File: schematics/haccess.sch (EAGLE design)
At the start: 41 parts, among them IC1 ATMEGA32U2-TQFP, IC2 REG1117, SW1 SPST_TACT-EVQQ2

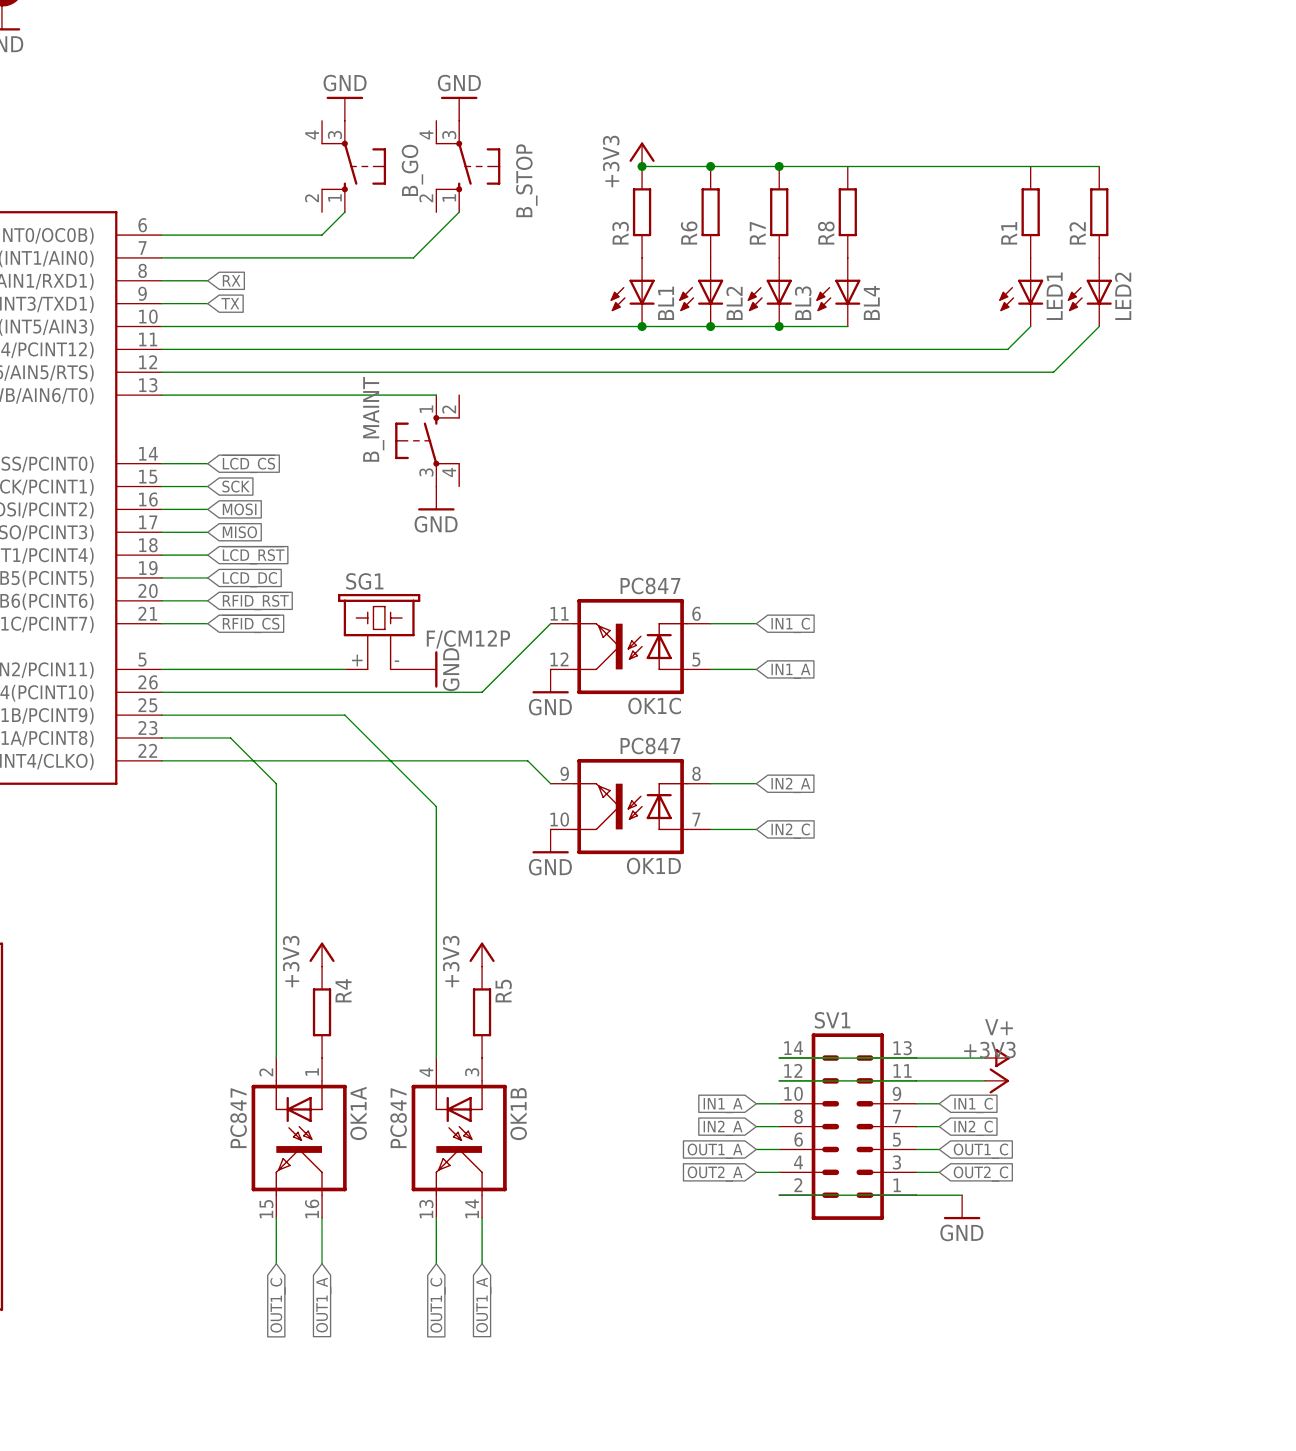
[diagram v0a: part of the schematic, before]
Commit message: First version of haccess PCB
Has components in correct places, some minimal routing.

Modified pattress plate to add correclty spaced holes for bolting haccess to plate.
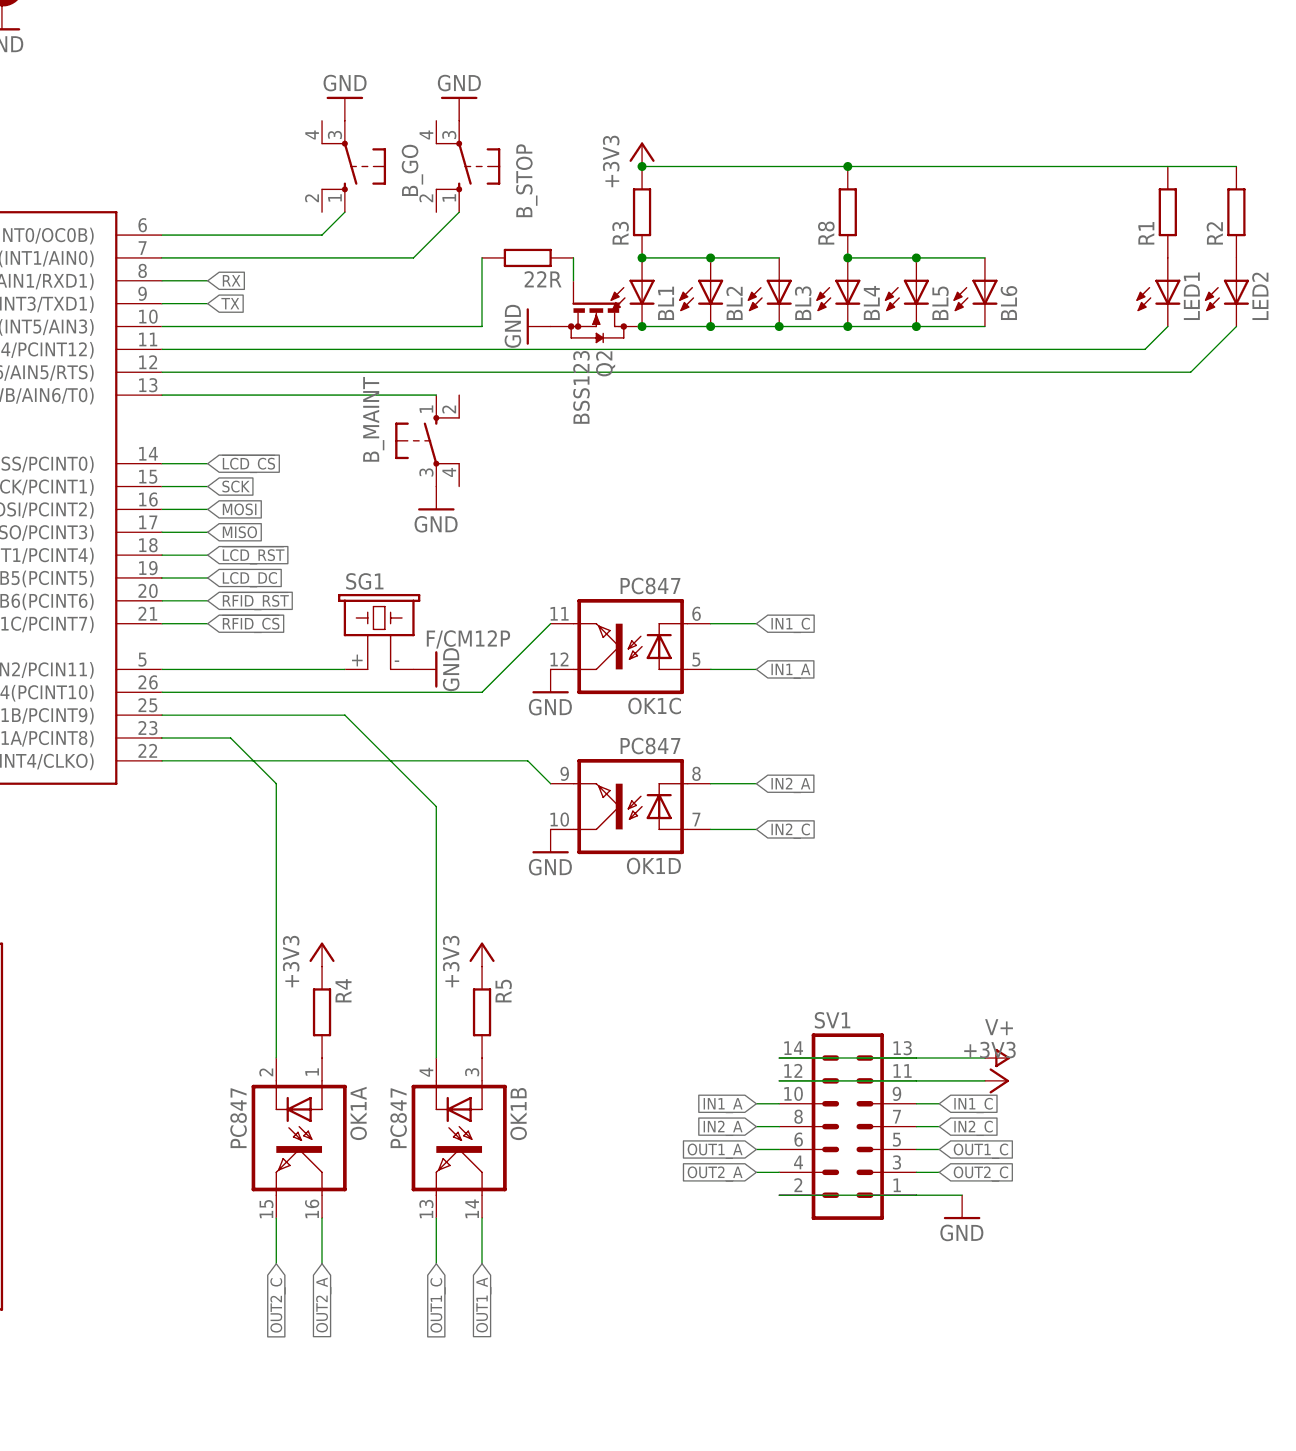
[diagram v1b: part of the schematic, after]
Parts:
- removed R6, R7: (no value), rcl:R-EU_R0805
- added 22R: (no value), rcl:R-EU_R0805
- added BL5, BL6: (no value), led:LEDCHIP-LED0805
- added Q2: BSS123, transistor-small-signal:BSS123
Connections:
- net +3V3: no longer R6.2, R7.2
- net GND: now also Q2.S
- net N$18: now also BL5.C, BL6.C, Q2.D; no longer IC1.PD4(INT5/AIN3)
- net N$19: now also BL2.A, BL3.A
- net N$21: now also 22R.2, IC1.PD4(INT5/AIN3); no longer BL2.A, R6.1
- net N$22: now also 22R.1, Q2.G; no longer BL3.A, R7.1
- net N$23: now also BL5.A, BL6.A
- net OUT1_A: no longer OK1A.COL
- net OUT1_C: no longer OK1A.EMIT
- net OUT2_A: now also OK1A.COL
- net OUT2_C: now also OK1A.EMIT
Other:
- moved on the sheet: LED1, LED2, R1, R2

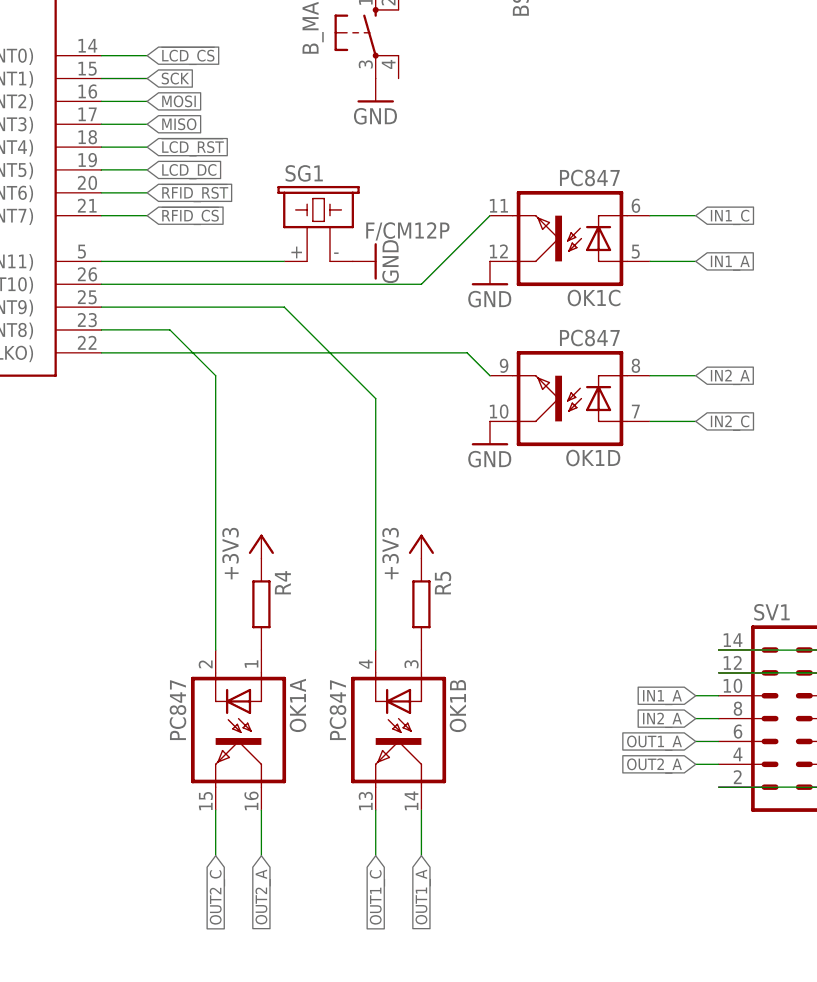
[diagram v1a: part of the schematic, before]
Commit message: Imported DXF of outline, got all important tuff into place, began routing
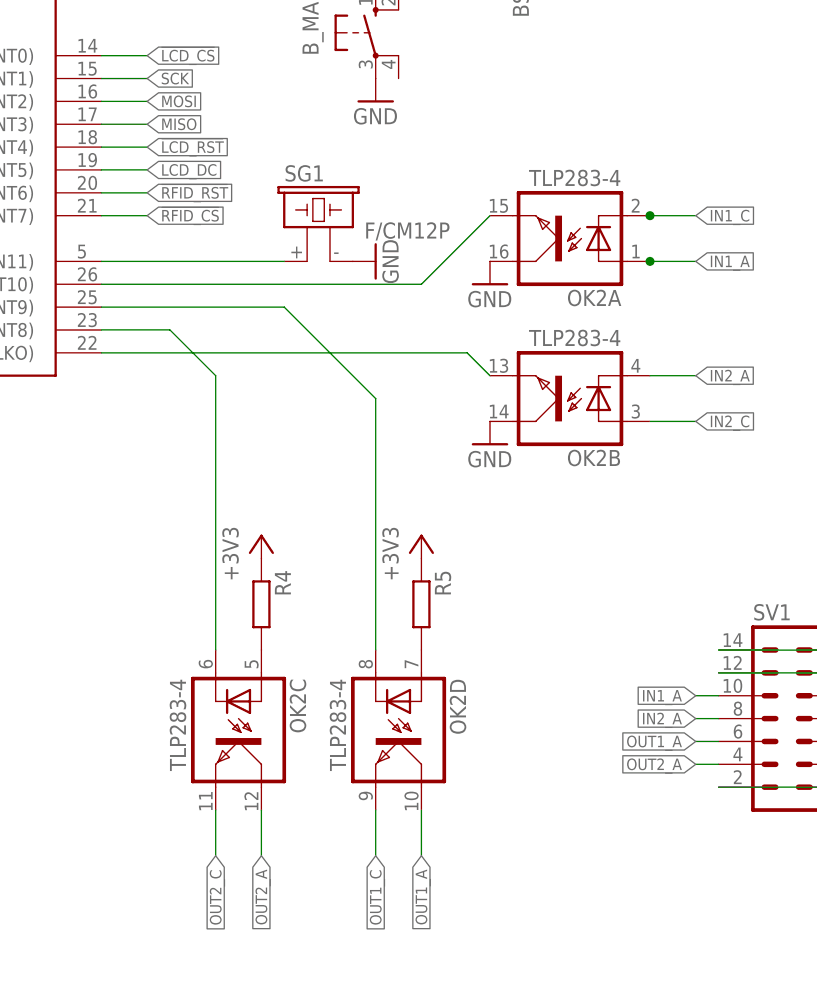
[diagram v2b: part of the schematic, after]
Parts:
- removed OK1: PC847, optocoupler:PC847
- added OK2: TLP283-4, optocoupler:TLP283-4
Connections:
- net GND: now also OK2A.COL, OK2B.COL; no longer OK1C.COL, OK1D.COL
- net IN1_A: now also OK2A.A; no longer OK1C.A
- net IN1_C: now also OK2A.C; no longer OK1C.C
- net IN2_A: now also OK2B.C; no longer OK1D.C
- net IN2_C: now also OK2B.A; no longer OK1D.A
- net N$10: now also OK2C.C; no longer OK1A.C
- net N$11: now also OK2D.C; no longer OK1B.C
- net N$13: now also OK2B.EMIT; no longer OK1D.EMIT
- net N$15: now also OK2A.EMIT; no longer OK1C.EMIT
- net N$16: now also OK2D.A, R5.2; no longer OK1A.A, R4.2
- net N$20: now also OK2C.A, R4.2; no longer OK1B.A, R5.2
- net OUT1_A: now also OK2D.COL; no longer OK1B.COL
- net OUT1_C: now also OK2D.EMIT; no longer OK1B.EMIT
- net OUT2_A: now also OK2C.COL; no longer OK1A.COL
- net OUT2_C: now also OK2C.EMIT; no longer OK1A.EMIT
